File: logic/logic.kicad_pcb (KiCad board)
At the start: 2 copper layers, 2 parts, among them J1 DIN41612_02x32_AC, U1 TPIC6595

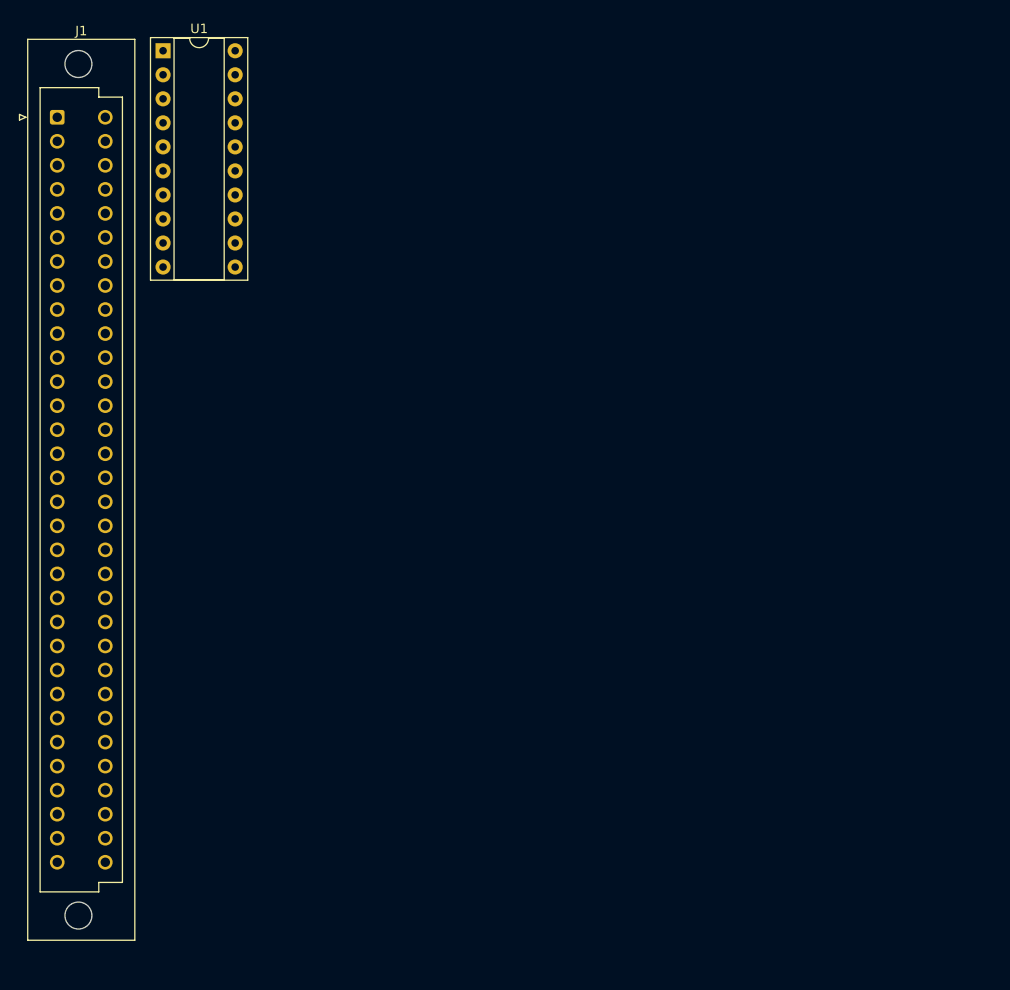
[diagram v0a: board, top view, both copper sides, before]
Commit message: Change to new 96-pin DIN-41612 schematic symbol in custom library
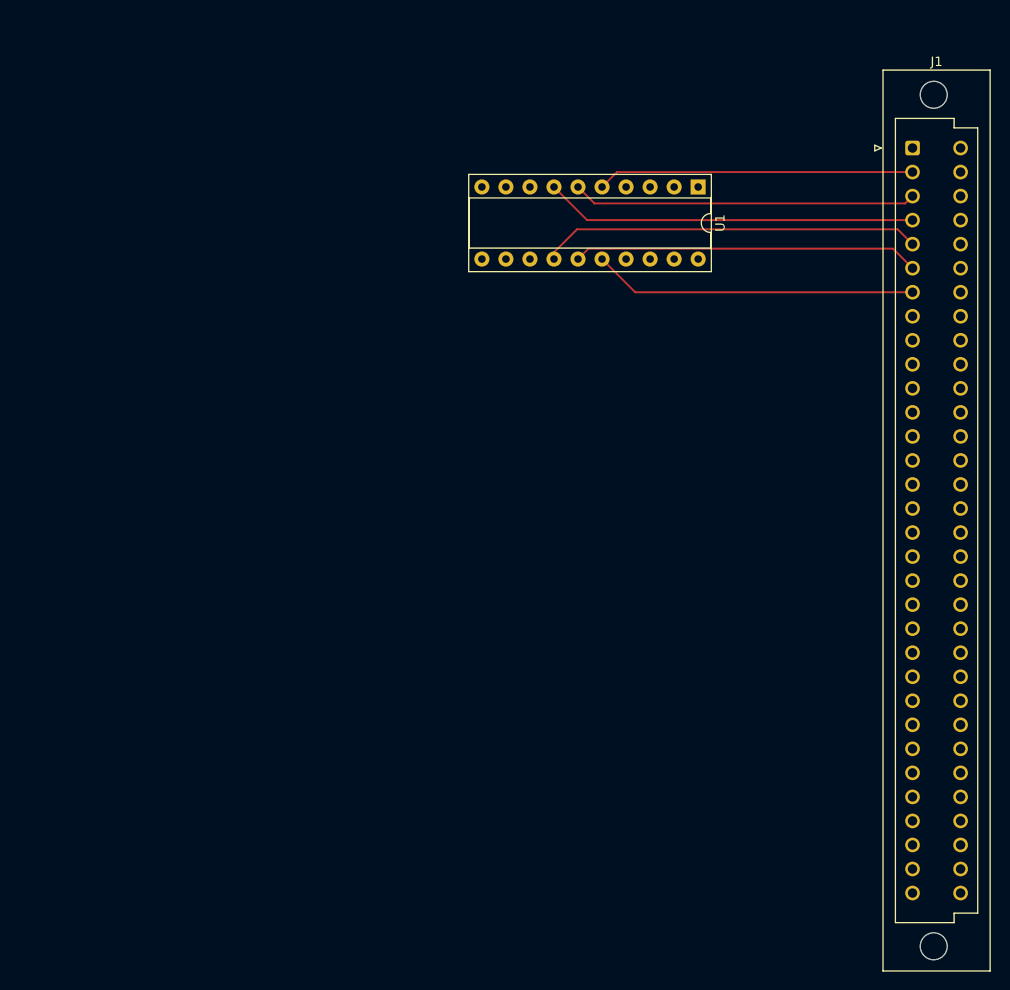
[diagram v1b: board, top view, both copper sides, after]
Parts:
- moved J1 90.5 mm to (136.7, 47.5)
- moved U1 58.4 mm to (114.0, 51.6), turned to -90 degrees
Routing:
- net /B1-4: track 0.00 -> 40.3 mm
- net /B1-3: track 0.00 -> 39.3 mm
- net /B1-5: track 0.00 -> 36.7 mm
- net /B1-2: track 0.00 -> 36.4 mm
- net /B1-6: track 0.00 -> 34.3 mm
- net /B1-1: track 0.00 -> 33.5 mm

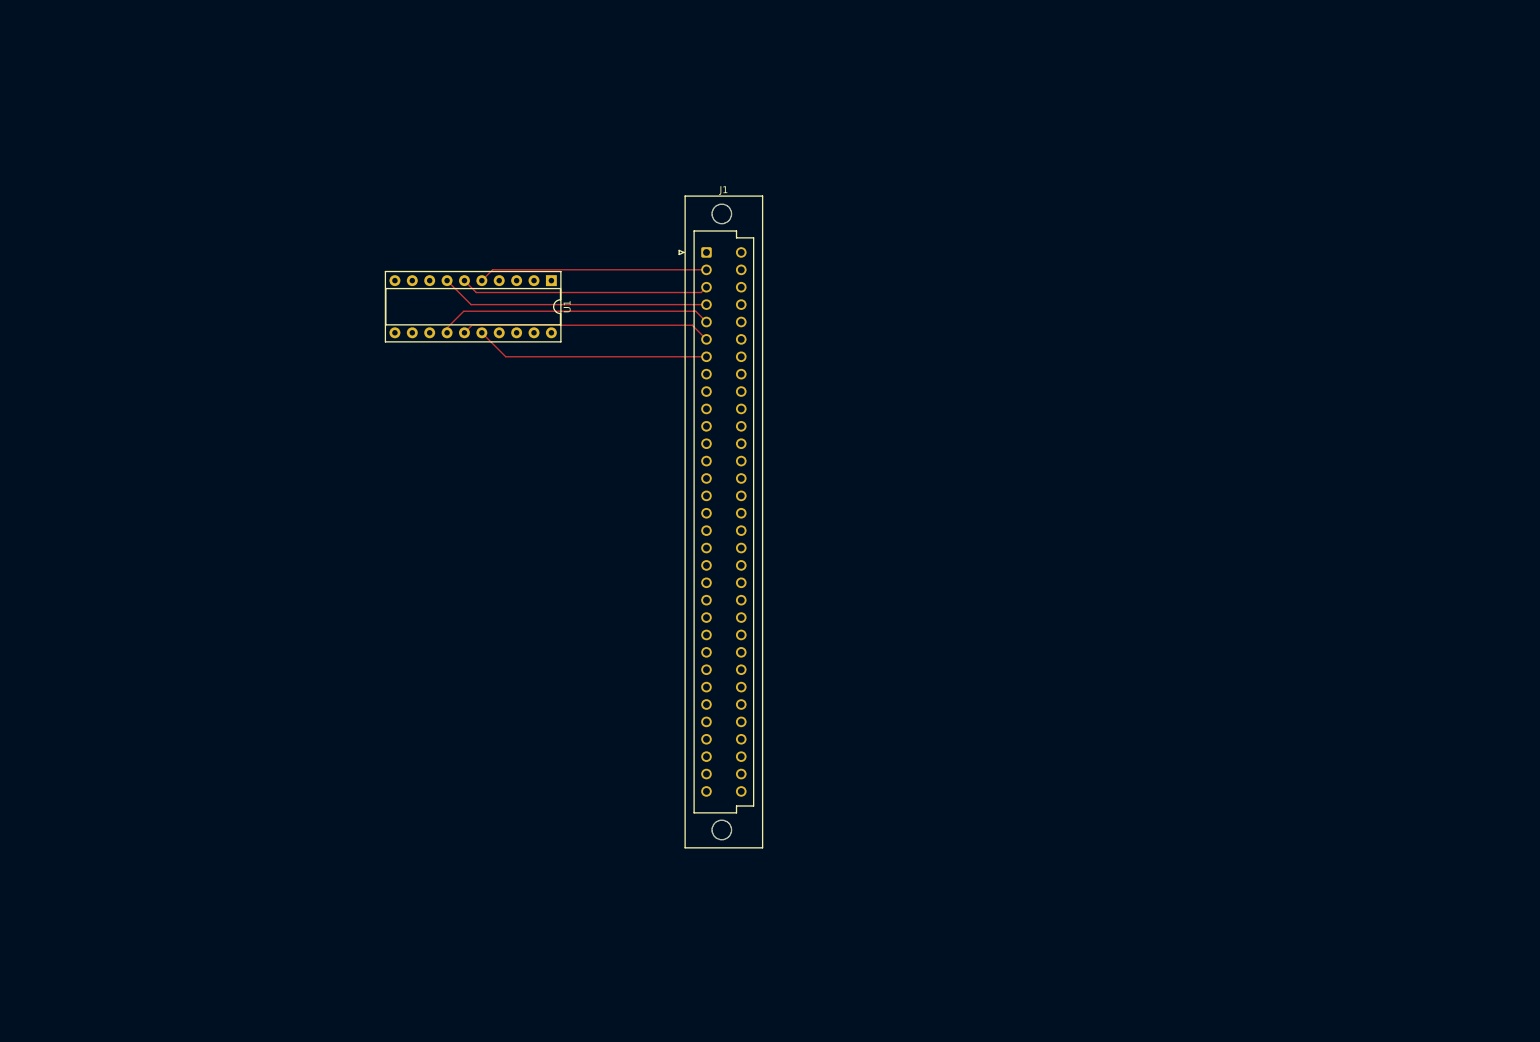
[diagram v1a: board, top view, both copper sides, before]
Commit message: Complete schematic. No DRC errors. Place components on PCB.
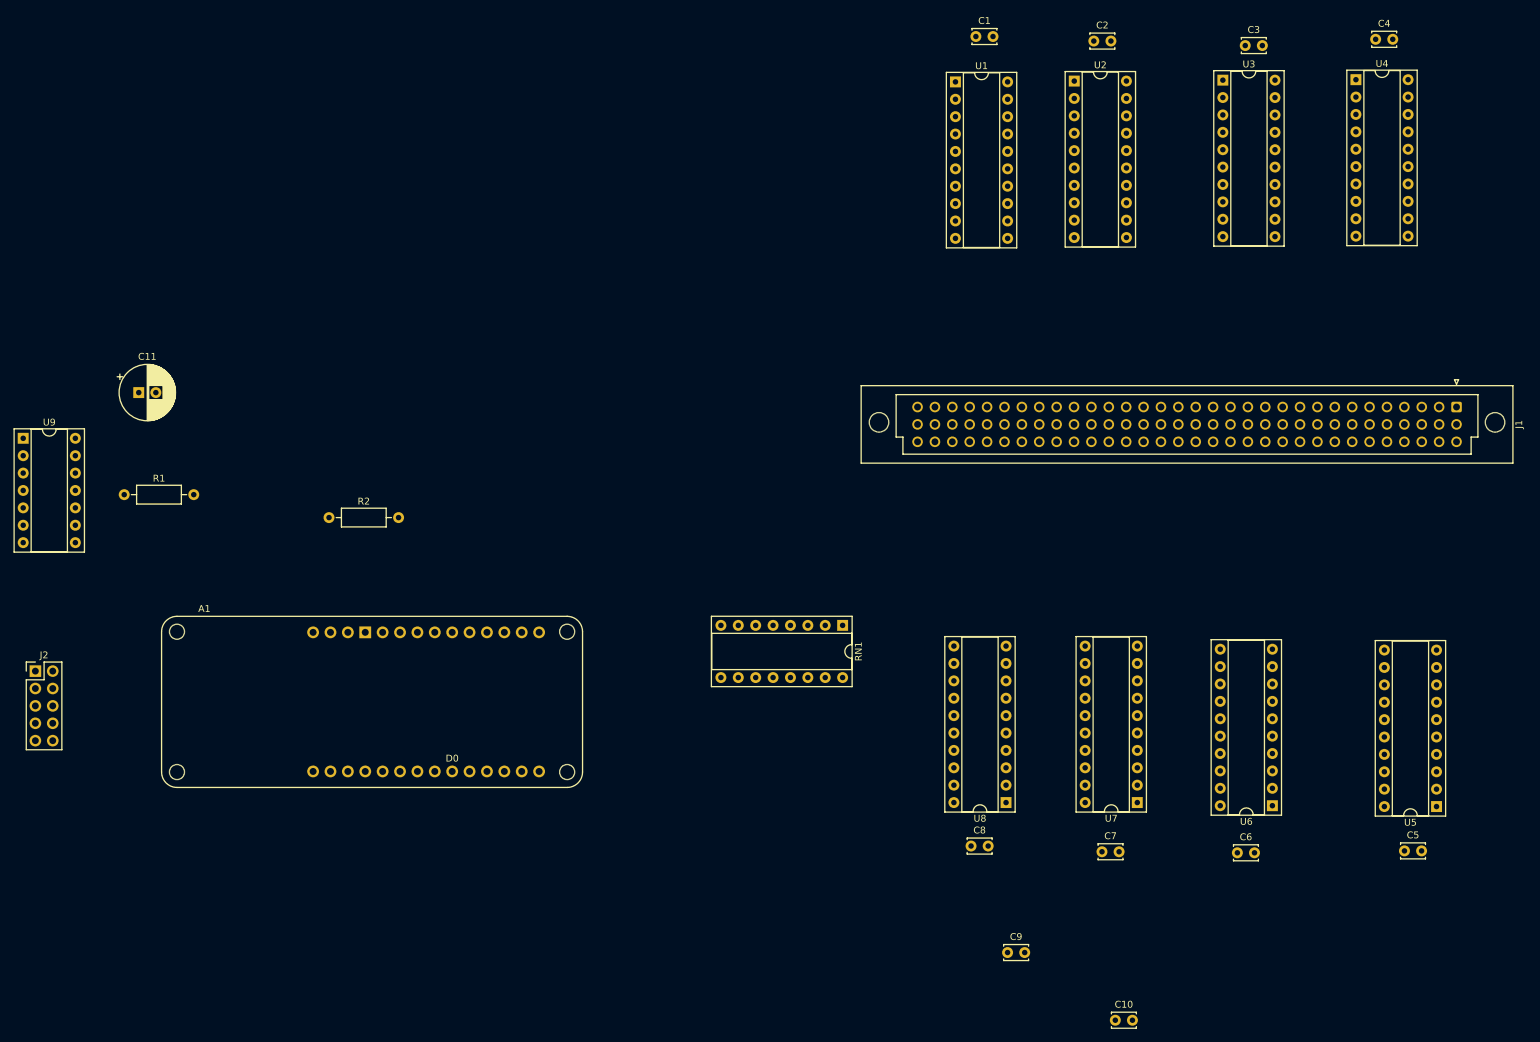
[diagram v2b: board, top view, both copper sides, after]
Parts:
- added A1: Arduino_MKR_WiFi_1010_Socket, arduino-library:Arduino_MKR_WiFi_1010_Socket, F.Cu at (59.3, 102.9)
- added C1: C, Capacitor_THT:C_Disc_D3.4mm_W2.1mm_P2.50mm, F.Cu at (176.0, 15.9)
- added C10: C, Capacitor_THT:C_Disc_D3.4mm_W2.1mm_P2.50mm, F.Cu at (196.4, 159.6)
- added C11: C, Capacitor_THT:CP_Radial_D8.0mm_P2.50mm, F.Cu at (53.7, 67.9)
- added C2: C, Capacitor_THT:C_Disc_D3.4mm_W2.1mm_P2.50mm, F.Cu at (193.3, 16.6)
- added C3: C, Capacitor_THT:C_Disc_D3.4mm_W2.1mm_P2.50mm, F.Cu at (215.4, 17.2)
- added C4: C, Capacitor_THT:C_Disc_D3.4mm_W2.1mm_P2.50mm, F.Cu at (234.4, 16.3)
- added C5: C, Capacitor_THT:C_Disc_D3.4mm_W2.1mm_P2.50mm, F.Cu at (238.6, 134.9)
- added C6: C, Capacitor_THT:C_Disc_D3.4mm_W2.1mm_P2.50mm, F.Cu at (214.2, 135.2)
- added C7: C, Capacitor_THT:C_Disc_D3.4mm_W2.1mm_P2.50mm, F.Cu at (194.5, 135.0)
- added C8: C, Capacitor_THT:C_Disc_D3.4mm_W2.1mm_P2.50mm, F.Cu at (175.3, 134.2)
- added C9: C, Capacitor_THT:C_Disc_D3.4mm_W2.1mm_P2.50mm, F.Cu at (180.7, 149.8)
- added J2: Conn_02x05_Odd_Even, Connector_PinHeader_2.54mm:PinHeader_2x05_P2.54mm_Vertical, F.Cu at (38.6, 108.6)
- added R1: R, Resistor_THT:R_Axial_DIN0207_L6.3mm_D2.5mm_P10.16mm_Horizontal, F.Cu at (51.6, 82.9)
- added R2: R, Resistor_THT:R_Axial_DIN0207_L6.3mm_D2.5mm_P10.16mm_Horizontal, F.Cu at (81.5, 86.2)
- added RN1: R_Pack08, Package_DIP:DIP-16_W7.62mm_Socket, F.Cu at (156.6, 102.0)
- added U2: TPIC6595, Package_DIP:DIP-20_W7.62mm_Socket, F.Cu at (190.4, 22.4)
- added U3: TPIC6595, Package_DIP:DIP-20_W7.62mm_Socket, F.Cu at (212.1, 22.3)
- added U4: TPIC6595, Package_DIP:DIP-20_W7.62mm_Socket, F.Cu at (231.6, 22.2)
- added U5: TPIC6595, Package_DIP:DIP-20_W7.62mm_Socket, F.Cu at (243.3, 128.4)
- added U6: TPIC6595, Package_DIP:DIP-20_W7.62mm_Socket, F.Cu at (219.4, 128.3)
- added U7: TPIC6595, Package_DIP:DIP-20_W7.62mm_Socket, F.Cu at (199.6, 127.8)
- added U8: TPIC6595, Package_DIP:DIP-20_W7.62mm_Socket, F.Cu at (180.4, 127.8)
- added U9: 74HC14, Package_DIP:DIP-14_W7.62mm_Socket, F.Cu at (36.9, 74.6)
- J1: value DIN41612_02x32_AC -> DIN41612_03x32_ABC; footprint Connector_DIN:DIN41612_R_2x32_Male_Vertical_THT -> Connector_DIN:DIN41612_R_3x32_Male_Vertical_THT
- moved J1 111.9 mm to (246.3, 70.1), turned to -90 degrees
- moved U1 65.8 mm to (173.1, 22.6), turned to 0 degrees
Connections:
- J1 pad a1: /B1-0 -> GND
- J1 pad a10: /B2-1 -> /B3-6
- J1 pad a11: /B2-2 -> /B3-5
- J1 pad a12: /B2-3 -> /B3-4
- J1 pad a13: /B2-4 -> /B3-3
- J1 pad a14: /B2-5 -> /B3-2
- J1 pad a15: /B2-6 -> /B3-1
- J1 pad a16: /B2-7 -> /B3-0
- J1 pad a17: /B3-0 -> /B2-7
- J1 pad a18: /B3-1 -> /B2-6
- J1 pad a19: /B3-2 -> /B2-5
- J1 pad a2: /B1-1 -> GND
- J1 pad a20: /B3-3 -> /B2-4
- J1 pad a21: /B3-4 -> /B2-3
- J1 pad a22: /B3-5 -> /B2-2
- J1 pad a23: /B3-6 -> /B2-1
- J1 pad a24: /B3-7 -> /B2-0
- J1 pad a25: /B4-0 -> /B1-7
- J1 pad a26: /B4-1 -> /B1-6
- J1 pad a27: /B4-2 -> /B1-5
- J1 pad a28: /B4-3 -> /B1-4
- J1 pad a29: /B4-4 -> /B1-3
- J1 pad a3: /B1-2 -> /B4-5
- J1 pad a30: /B4-5 -> /B1-2
- J1 pad a31: GND -> /B1-1
- J1 pad a32: GND -> /B1-0
- J1 pad a4: /B1-3 -> /B4-4
- J1 pad a5: /B1-4 -> /B4-3
- J1 pad a6: /B1-5 -> /B4-2
- J1 pad a7: /B1-6 -> /B4-1
- J1 pad a8: /B1-7 -> /B4-0
- J1 pad a9: /B2-0 -> /B3-7
- J1 pad c1: GND -> /B5-0
- J1 pad c10: /B7-6 -> /B6-1
- J1 pad c11: /B7-5 -> /B6-2
- J1 pad c12: /B7-4 -> /B6-3
- J1 pad c13: /B7-3 -> /B6-4
- J1 pad c14: /B7-2 -> /B6-5
- J1 pad c15: /B7-1 -> /B6-6
- J1 pad c16: /B7-0 -> /B6-7
- J1 pad c17: /B6-7 -> /B7-0
- J1 pad c18: /B6-6 -> /B7-1
- J1 pad c19: /B6-5 -> /B7-2
- J1 pad c2: GND -> /B5-1
- J1 pad c20: /B6-4 -> /B7-3
- J1 pad c21: /B6-3 -> /B7-4
- J1 pad c22: /B6-2 -> /B7-5
- J1 pad c23: /B6-1 -> /B7-6
- J1 pad c24: /B6-0 -> /B7-7
- J1 pad c25: /B5-7 -> /B8-0
- J1 pad c26: /B5-6 -> /B8-1
- J1 pad c27: /B5-5 -> /B8-2
- J1 pad c28: /B5-4 -> /B8-3
- J1 pad c29: /B5-3 -> /B8-4
- J1 pad c3: /B8-5 -> /B5-2
- J1 pad c30: /B5-2 -> /B8-5
- J1 pad c31: /B5-1 -> GND
- J1 pad c32: /B5-0 -> GND
- J1 pad c4: /B8-4 -> /B5-3
- J1 pad c5: /B8-3 -> /B5-4
- J1 pad c6: /B8-2 -> /B5-5
- J1 pad c7: /B8-1 -> /B5-6
- J1 pad c8: /B8-0 -> /B5-7
- J1 pad c9: /B7-7 -> /B6-0
- U1 pad 3: Net-(A1-D8_MOSI) -> /COPI
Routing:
- net /B1-4: track 40.3 -> 0.00 mm
- net /B1-3: track 39.3 -> 0.00 mm
- net /B1-5: track 36.7 -> 0.00 mm
- net /B1-2: track 36.4 -> 0.00 mm
- net /B1-6: track 34.3 -> 0.00 mm
- net /B1-1: track 33.5 -> 0.00 mm

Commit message: Update schematic and PCB with HV supply footprint
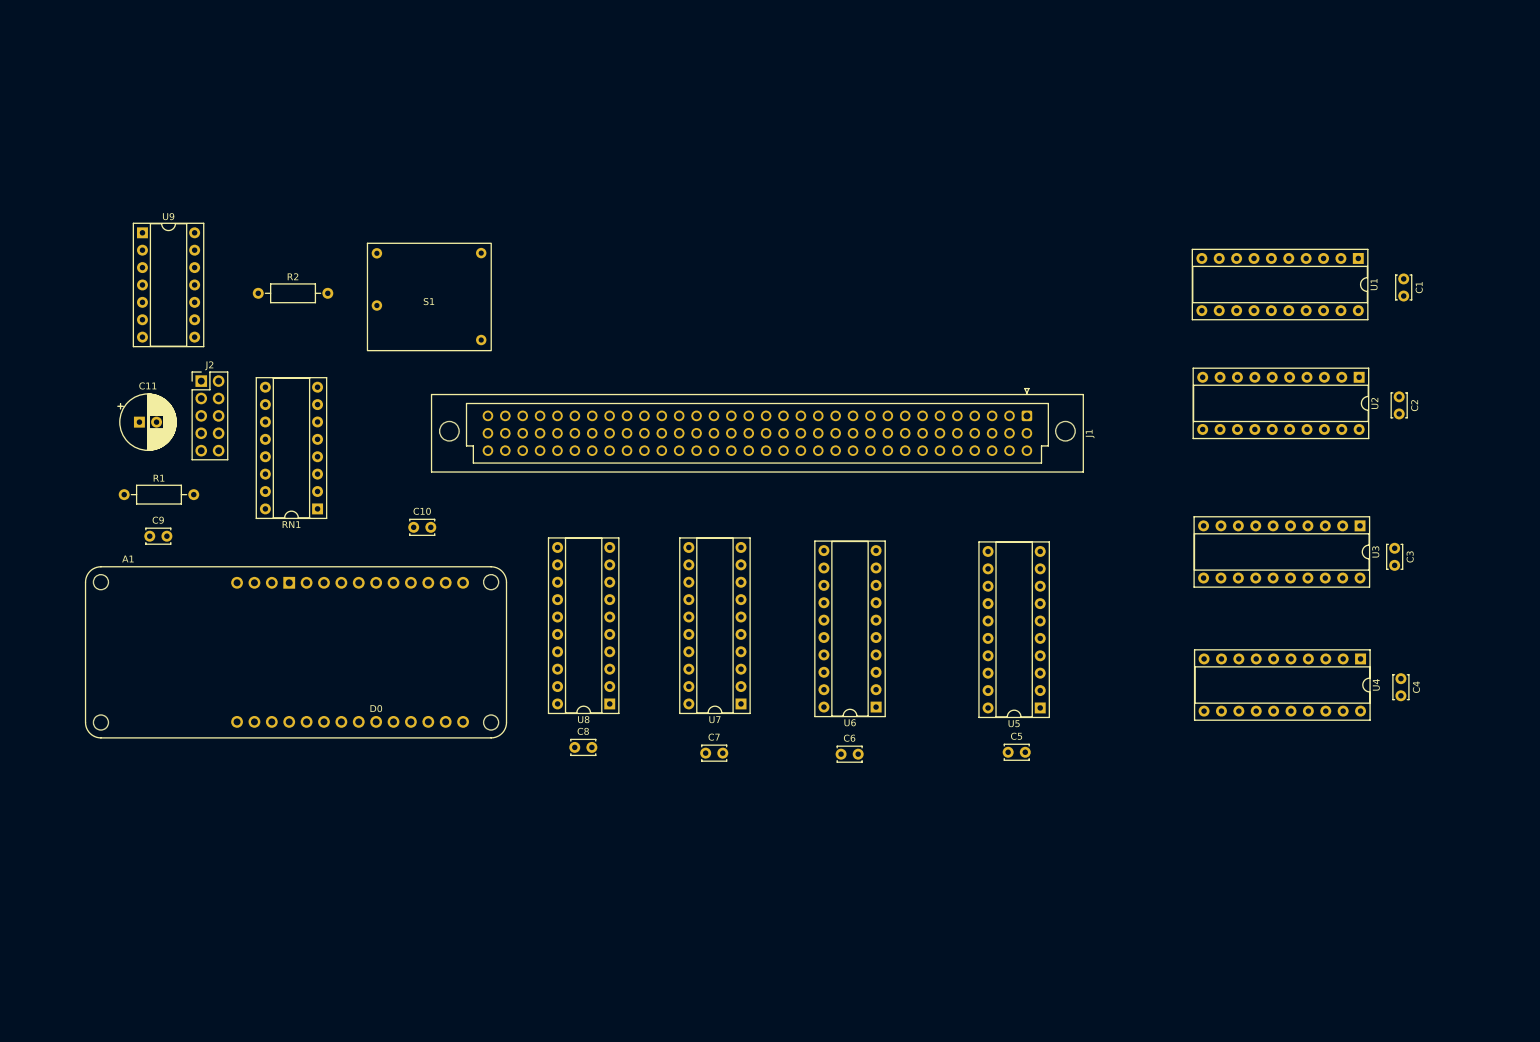
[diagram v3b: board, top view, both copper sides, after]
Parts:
- added S1: ~, NixComp:NCH8200HV, F.Cu at (96.1, 55.2)
- moved C9 139.3 mm to (55.3, 88.9)
- moved C10 125.3 mm to (93.9, 87.6)
- moved C4 93.5 mm to (238.1, 109.7), turned to -90 degrees
- moved U4 84.6 mm to (232.2, 106.9), turned to -90 degrees
- moved RN1 78.6 mm to (79.9, 84.9), turned to 180 degrees
- moved C3 76.6 mm to (237.2, 90.7), turned to -90 degrees
- moved C1 71.8 mm to (238.5, 51.3), turned to -90 degrees
- moved C2 68.5 mm to (237.9, 68.6), turned to -90 degrees
- moved U3 68.1 mm to (232.2, 87.4), turned to -90 degrees
- moved U1 64.3 mm to (231.9, 48.4), turned to -90 degrees
- moved J1 62.8 mm to (183.5, 71.3)
- moved U2 60.0 mm to (232.0, 65.7), turned to -90 degrees
- moved C5 59.7 mm to (180.8, 120.5)
- moved C6 59.7 mm to (156.3, 120.8)
- moved C7 59.7 mm to (136.6, 120.6)
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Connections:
- J1 pad a1: GND -> VCC
- J1 pad a2: GND -> VCC
- J1 pad b1: GND -> Net-(J1-Pin_b1)
- J1 pad b2: GND -> Net-(J1-Pin_b1)
- J1 pad b25: GND -> Net-(J1-Pin_b25)
- J1 pad b26: GND -> Net-(J1-Pin_b26)
- J1 pad b3: GND -> Net-(J1-Pin_b1)
- J1 pad b4: GND -> Net-(J1-Pin_b1)
- J1 pad b5: GND -> Net-(J1-Pin_b1)
- J1 pad b6: GND -> Net-(J1-Pin_b1)
- J1 pad b7: GND -> Net-(J1-Pin_b1)
- RN1 pad 1: unconnected-(RN1-R1.1-Pad1) -> Net-(J1-Pin_b25)
- RN1 pad 2: unconnected-(RN1-R2.1-Pad2) -> Net-(J1-Pin_b26)

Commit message: Additional minor tweaking
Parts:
- moved S1 113.9 mm to (210.0, 56.0)
- moved U1 108.5 mm to (123.8, 39.2), turned to 0 degrees
- moved C1 104.6 mm to (134.4, 41.1), turned to 90 degrees
- moved U2 94.7 mm to (141.1, 39.1), turned to 0 degrees
- moved C2 90.2 mm to (151.9, 41.1), turned to 90 degrees
- moved U3 86.6 mm to (160.8, 38.3), turned to 0 degrees
- moved U4 86.1 mm to (180.2, 38.3), turned to 0 degrees
- moved C4 83.6 mm to (191.3, 40.5), turned to 90 degrees
- moved C3 82.8 mm to (171.5, 40.4), turned to 90 degrees
- moved C9 79.1 mm to (119.0, 42.0), turned to 90 degrees
- moved A1 71.3 mm to (94.1, 41.0), turned to -90 degrees
- moved R1 55.0 mm to (103.0, 63.2), turned to 90 degrees
- moved C11 54.6 mm to (100.5, 44.0)
- moved U9 54.3 mm to (108.4, 39.9)
- moved J2 46.5 mm to (90.1, 104.0), turned to -90 degrees
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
